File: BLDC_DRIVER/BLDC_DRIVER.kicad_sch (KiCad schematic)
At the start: 0 parts

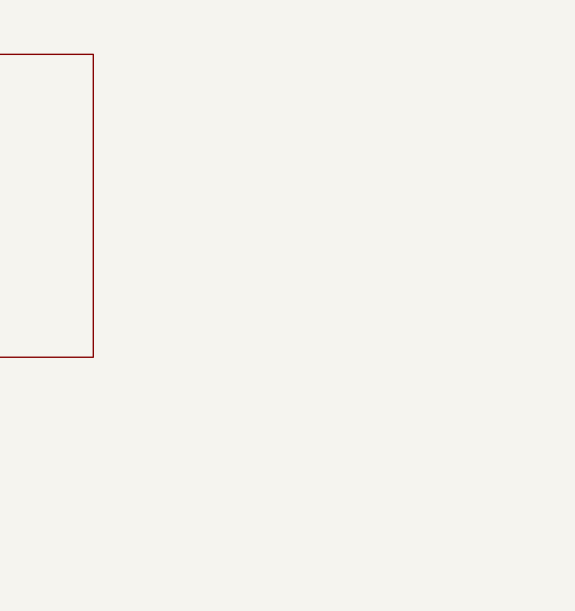
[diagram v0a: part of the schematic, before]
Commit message: added gate driver and igbt's
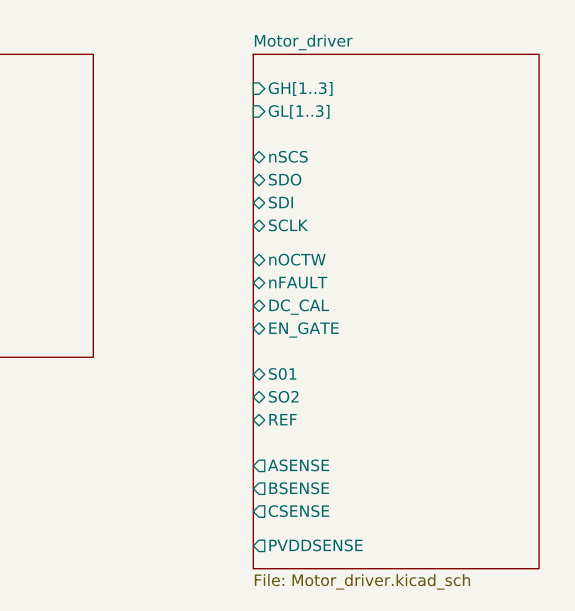
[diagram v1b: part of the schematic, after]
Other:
- added sheet Motor_driver (Motor_driver.kicad_sch)
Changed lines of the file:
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@@
 	(paper "A4")
+	(sheet
+		(at 157.48 36.83)
+		(size 31.75 57.15)
+		(exclude_from_sim no)
+		(in_bom yes)
+		(on_board yes)
+		(dnp no)
+		(fields_autoplaced yes)
+		(stroke
+			(width 0.1524)
+			(type solid)
+		)
+		(fill
+			(color 0 0 0 0.0000)
+		)
+		(property "Sheetname" "Motor_driver"
+			(at 157.48 36.1184 0)
+			(effects
+				(font
+					(size 1.27 1.27)
+				)
+				(justify left bottom)
+			)
+		)
+		(property "Sheetfile" "Motor_driver.kicad_sch"
+			(at 157.48 94.5646 0)
+			(effects
+				(font
+					(size 1.27 1.27)
+				)
+				(justify left top)
+			)
+		)
+		(pin "GH[1..3]" input
+			(at 157.48 40.64 180)
+			(effects
+				(font
+					(size 1.27 1.27)
+				)
+				(justify left)
+			)
+		)
+		(pin "GL[1..3]" input
+			(at 157.48 43.18 180)
+			(effects
+				(font
+					(size 1.27 1.27)
+				)
+				(justify left)
+			)
+		)
+		(pin "nFAULT" bidirectional
+			(at 157.48 62.23 180)
+			(effects
+				(font
+					(size 1.27 1.27)
+				)
+				(justify left)
+			)
+		)
+		(pin "SDO" bidirectional
+			(at 157.48 50.8 180)
+			(effects
+				(font
+					(size 1.27 1.27)
+				)
+				(justify left)
+			)
+		)
+		(pin "REF" bidirectional
+			(at 157.48 77.47 180)
+			(effects
+				(font
+					(size 1.27 1.27)
+				)
+				(justify left)
+			)
+		)
+		(pin "nSCS" bidirectional
+			(at 157.48 48.26 180)
+			(effects
+				(font
+					(size 1.27 1.27)
+				)
+				(justify left)
+			)
+		)
+		(pin "nOCTW" bidirectional
+			(at 157.48 59.69 180)
+			(effects
+				(font
+					(size 1.27 1.27)
+				)
+				(justify left)
+			)
+		)
+		(pin "SCLK" bidirectional
+			(at 157.48 55.88 180)
+			(effects
+				(font
+					(size 1.27 1.27)
+				)
+				(justify left)
+			)
+		)
+		(pin "DC_CAL" bidirectional
+			(at 157.48 64.77 180)
+			(effects
+				(font
+					(size 1.27 1.27)
+				)
+				(justify left)
+			)
+		)
+		(pin "SDI" bidirectional
+			(at 157.48 53.34 180)
+			(effects
+				(font
+					(size 1.27 1.27)
+				)
+				(justify left)
+			)
+		)
+		(pin "EN_GATE" bidirectional
+			(at 157.48 67.31 180)
+			(effects
+				(font
+					(size 1.27 1.27)
+				)
+				(justify left)
+			)
+		)
+		(pin "BSENSE" output
+			(at 157.48 85.09 180)
+			(effects
+				(font
+					(size 1.27 1.27)
+				)
+				(justify left)
+			)
+		)
+		(pin "S01" bidirectional
+			(at 157.48 72.39 180)
+			(effects
+				(font
+					(size 1.27 1.27)
+				)
+				(justify left)
+			)
+		)
+		(pin "ASENSE" output
+			(at 157.48 82.55 180)
+			(effects
+				(font
+					(size 1.27 1.27)
+				)
+				(justify left)
+			)
+		)
+		(pin "SO2" bidirectional
+			(at 157.48 74.93 180)
+			(effects
+				(font
+					(size 1.27 1.27)
+				)
+				(justify left)
+			)
+		)
+		(pin "CSENSE" output
+			(at 157.48 87.63 180)
+			(effects
+				(font
+					(size 1.27 1.27)
+				)
+				(justify left)
+			)
+		)
+		(pin "PVDDSENSE" output
+			(at 157.48 91.44 180)
+			(effects
+				(font
+					(size 1.27 1.27)
+				)
+				(justify left)
+			)
+		)
+		(instances
+			(project "BLDC_DRIVER"
+				(path "/3fb7c58e-7fa7-4c2f-8afc-969dd7f24a74"
+					(page "4")
+				)
+			)
+		)
+	)
 	(sheet
 		(at 33.655 35.56)

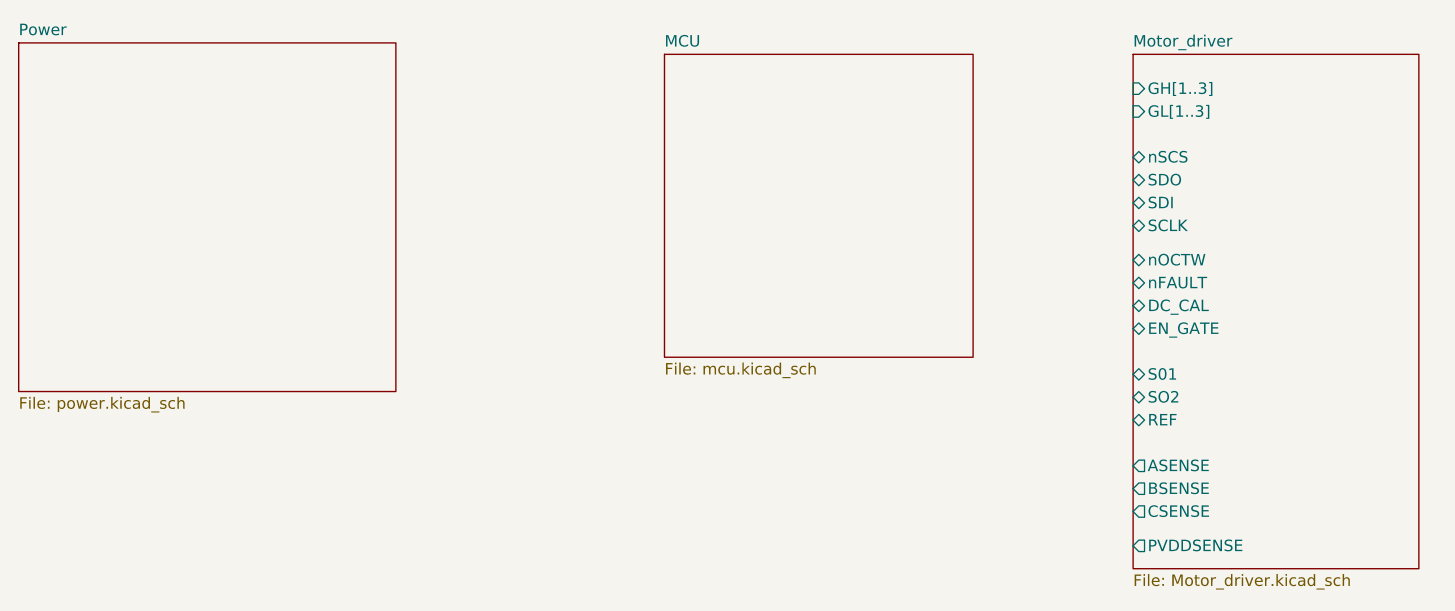
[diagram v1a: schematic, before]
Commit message: ldo added
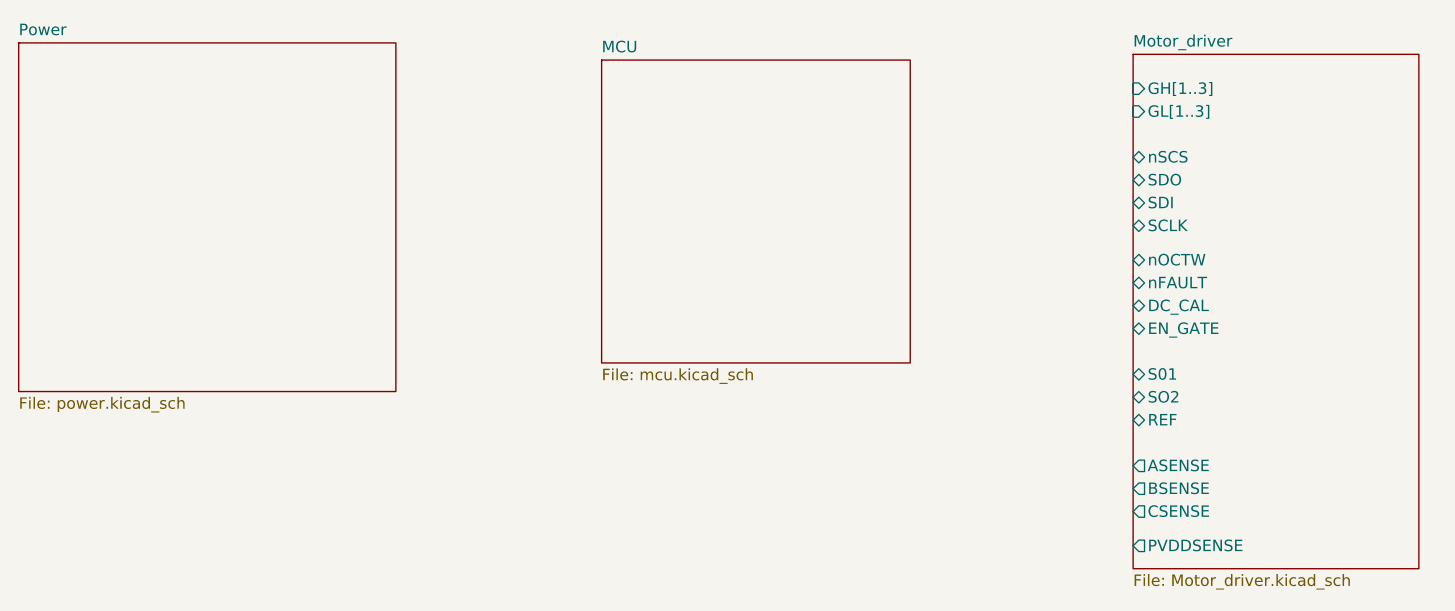
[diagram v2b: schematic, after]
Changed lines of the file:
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@@
 	)
 	(sheet
-		(at 105.41 36.83)
+		(at 98.425 37.465)
 		(size 34.29 33.655)
 		(exclude_from_sim no)
@@
 		)
 		(property "Sheetname" "MCU"
-			(at 105.41 36.1184 0)
+			(at 98.425 36.7534 0)
 			(effects
 				(font
@@
 		)
 		(property "Sheetfile" "mcu.kicad_sch"
-			(at 105.41 71.0696 0)
+			(at 98.425 71.7046 0)
 			(effects
 				(font
